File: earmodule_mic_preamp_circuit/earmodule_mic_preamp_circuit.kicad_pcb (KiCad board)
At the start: 2 copper layers, 31.2 x 25.4 mm, 52 parts, among them U100 ADA4661-2ARMZ, U200 AD8476ARMZ, U300 AD8476ARMZ, U400 TITLV71210

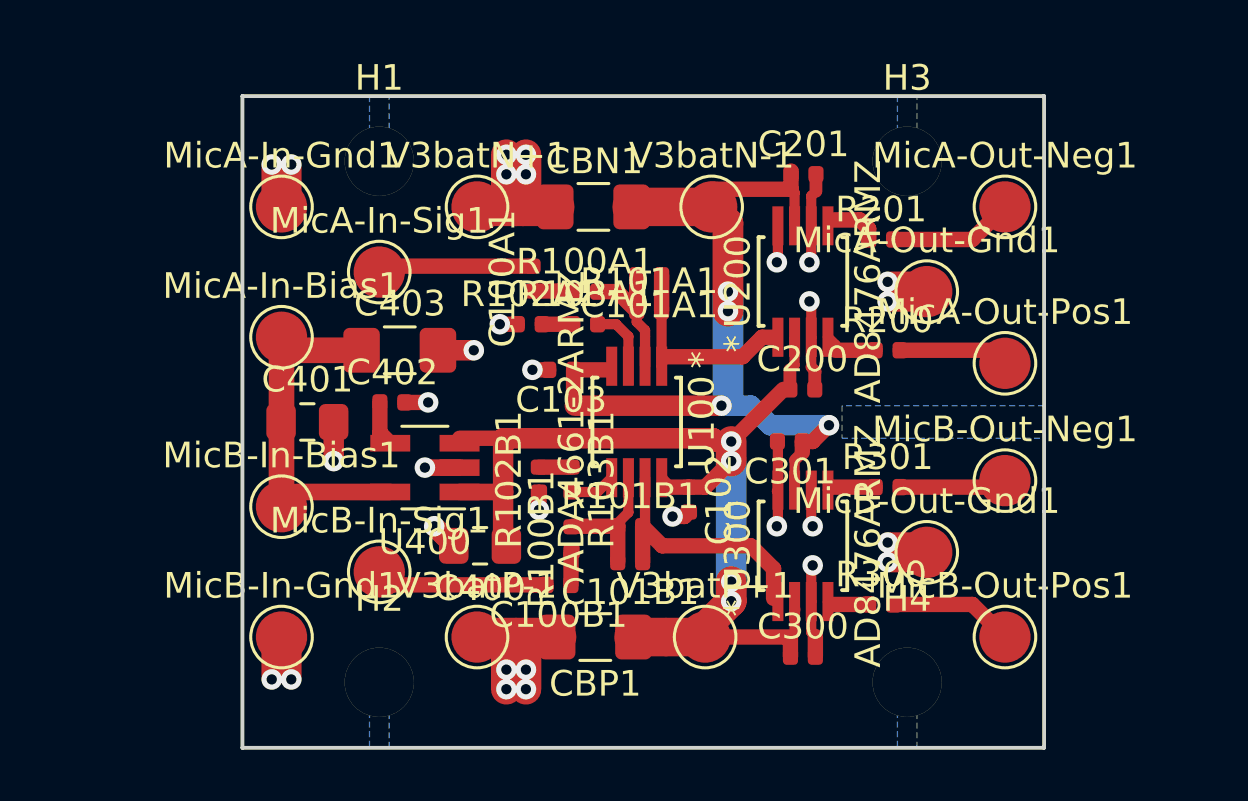
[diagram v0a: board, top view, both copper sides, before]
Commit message: Shrink and position silkscreen
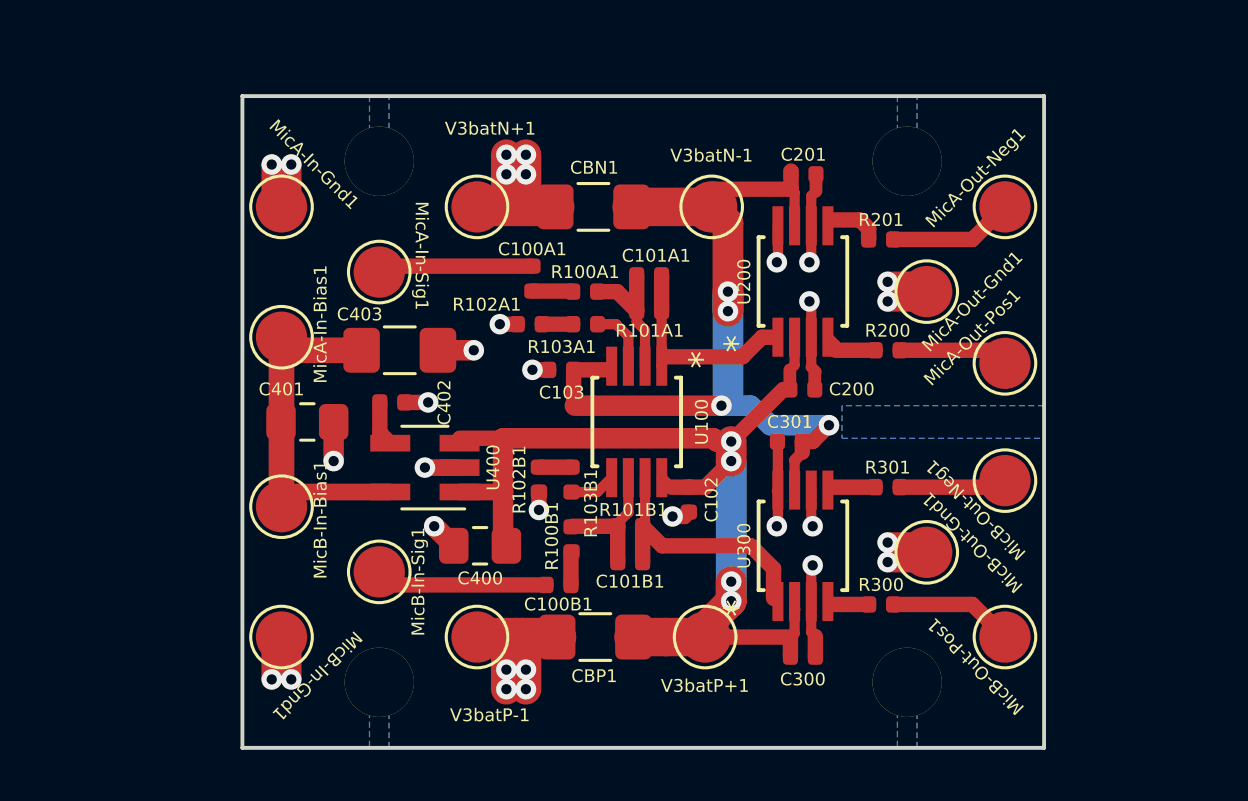
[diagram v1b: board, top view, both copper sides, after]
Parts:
-  : renamed from H4
-  : renamed from H1
-  : renamed from H3
-  : renamed from H2
- U100: value ADA4661-2ARMZ -> RM_8_ADI
- U200, U300: value AD8476ARMZ -> RM_8_ADI

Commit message: Rearranged regulator layout for better co-location of parts. Cleaned up interface names.
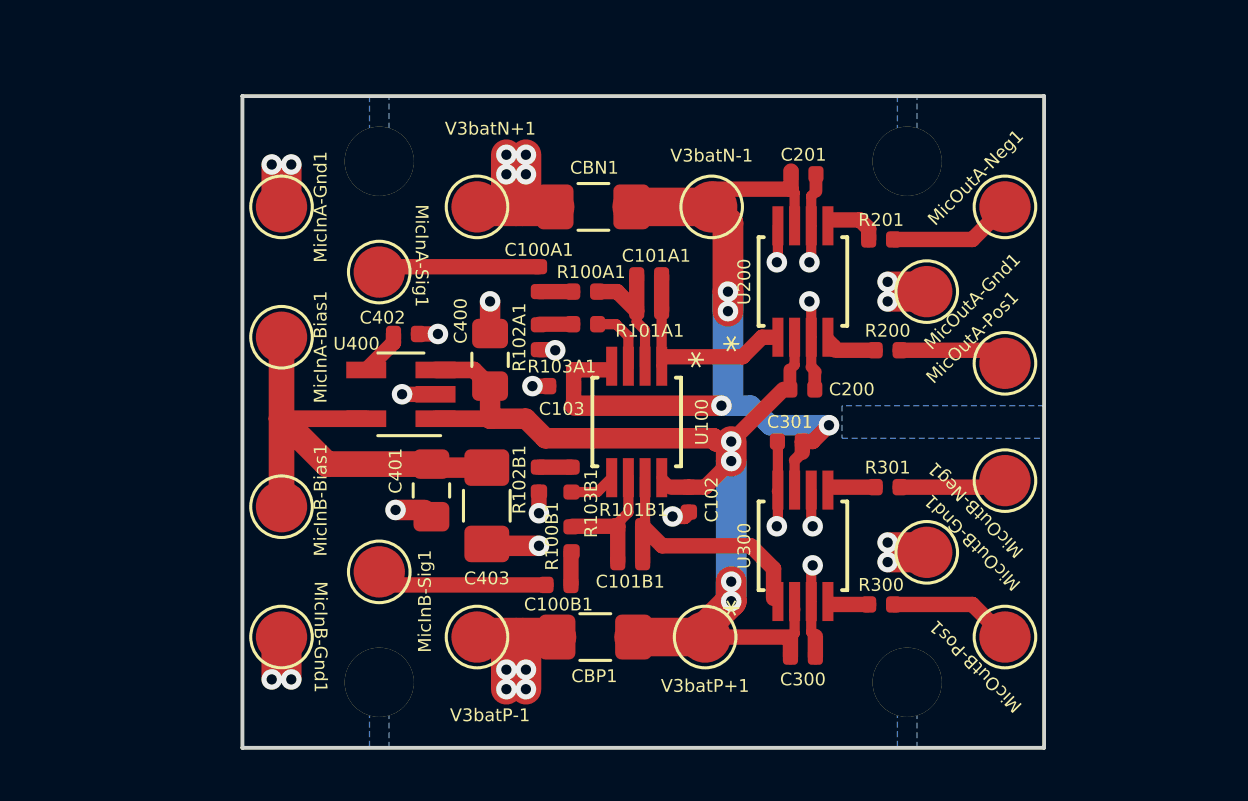
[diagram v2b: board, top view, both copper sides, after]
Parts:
- H1, H2, H3, H4: renamed from  
- U100: value RM_8_ADI -> ADA4661-2ARMZ
- U200, U300: value RM_8_ADI -> AD8476ARMZ
- moved C400 7.26 mm to (122.4, 82.2), turned to 90 degrees
- moved C403 6.94 mm to (122.3, 87.8), turned to 270 degrees
- moved C401 5.52 mm to (120.1, 87.2), turned to 270 degrees
- moved U400 3.00 mm to (119.0, 83.5)
- moved C402 2.72 mm to (119.1, 81.2)
- moved C103 0.64 mm to (125.2, 83.2)
- moved R102A1 0.62 mm to (124.3, 81.3), turned to 90 degrees
- moved C100A1 0.26 mm to (124.3, 79.0)
- renumbered MicA-In-Bias1 to MicInA-Bias1, MicA-In-Gnd1 to MicInA-Gnd1, MicA-In-Sig1 to MicInA-Sig1, MicB-In-Bias1 to MicInB-Bias1, MicB-In-Gnd1 to MicInB-Gnd1, MicB-In-Sig1 to MicInB-Sig1, MicA-Out-Gnd1 to MicOutA-Gnd1, MicA-Out-Neg1 to MicOutA-Neg1, MicA-Out-Pos1 to MicOutA-Pos1, MicB-Out-Gnd1 to MicOutB-Gnd1, MicB-Out-Neg1 to MicOutB-Neg1, MicB-Out-Pos1 to MicOutB-Pos1
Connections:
- net MicA-In-Bias renamed MicInA-Bias
- net MicA-In-Gnd renamed MicInA-Gnd
- net MicA-In-Sig renamed MicInA-Sig
- net MicA-Out-Neg renamed MicOutA-Neg
- net MicA-Out-Pos renamed MicOutA-Pos
- net MicB-In-Sig renamed MicInB-Sig
- net MicB-Out-Neg renamed MicOutB-Neg
- net MicB-Out-Pos renamed MicOutB-Pos
- net V3batN- renamed V3neg
- net V3batP+ renamed V3pos
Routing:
- net MicInA-Bias: track 14.4 -> 19.5 mm
- net V3pos: track 51.4 -> 49.1 mm

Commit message: Enlarged board and wire solder pad sizes. Added small decoupling caps in bias circuit. Finalized naming, numbering, and placement of text.
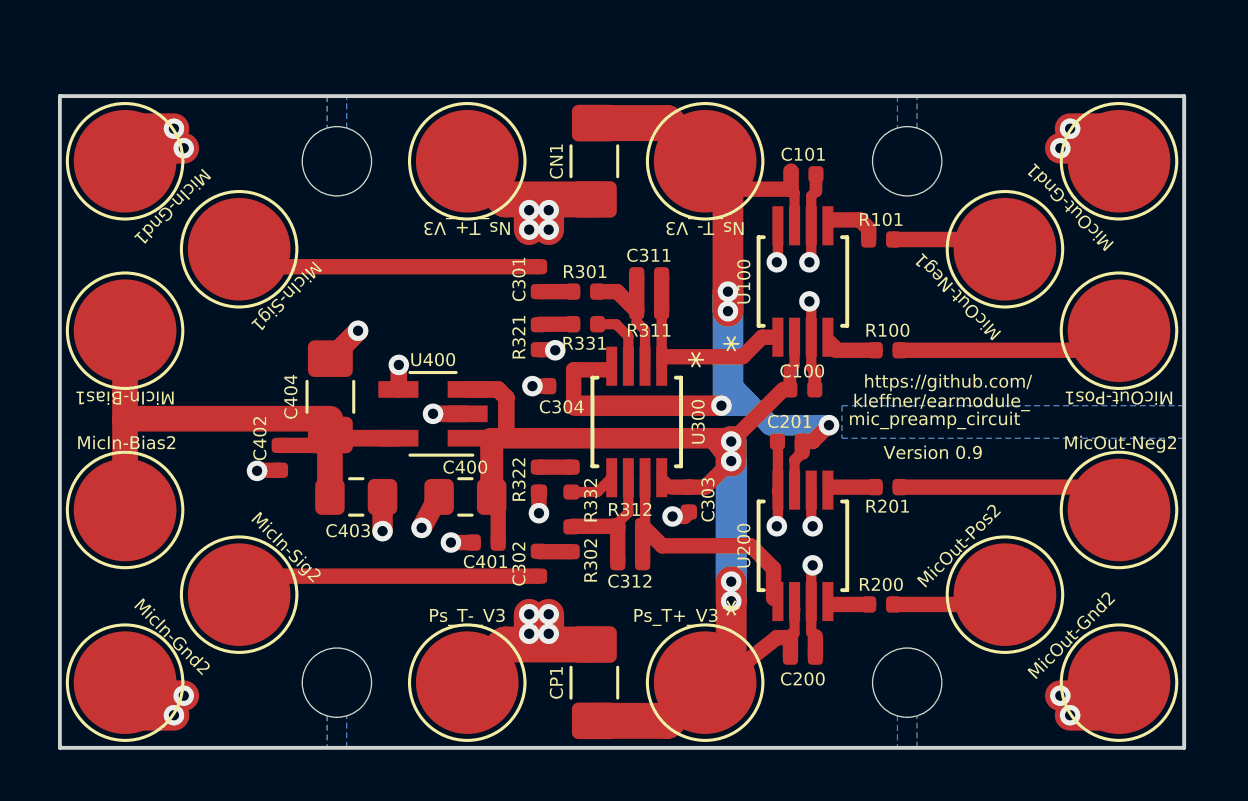
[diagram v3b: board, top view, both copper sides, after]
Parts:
- removed MicInA-Bias1, MicInA-Gnd1, MicInA-Sig1, MicInB-Bias1, MicInB-Gnd1, MicInB-Sig1, MicOutA-Gnd1, MicOutA-Neg1, MicOutA-Pos1, MicOutB-Gnd1, MicOutB-Neg1, MicOutB-Pos1, V3batN+1, V3batN-1, V3batP+1, V3batP-1: Conn_01x01_Male, TestPoint:TestPoint_Pad_D2.0mm
- added C401: 0.1uF, Capacitor_SMD:C_0402_1005Metric, F.Cu at (122.3, 89.3)
- added MicIn-Bias1: Conn_01x01_Male, TestPoint:TestPoint_Pad_D4.0mm, F.Cu at (108.2, 81.0)
- added MicIn-Bias2: Conn_01x01_Male, TestPoint:TestPoint_Pad_D4.0mm, F.Cu at (108.2, 88.0)
- added MicIn-Gnd1: Conn_01x01_Male, TestPoint:TestPoint_Pad_D4.0mm, F.Cu at (108.2, 74.4)
- added MicIn-Gnd2: Conn_01x01_Male, TestPoint:TestPoint_Pad_D4.0mm, F.Cu at (108.2, 94.7)
- added MicIn-Sig1: Conn_01x01_Male, TestPoint:TestPoint_Pad_D4.0mm, F.Cu at (112.6, 77.9)
- added MicIn-Sig2: Conn_01x01_Male, TestPoint:TestPoint_Pad_D4.0mm, F.Cu at (112.6, 91.3)
- added MicOut-Gnd1: Conn_01x01_Male, TestPoint:TestPoint_Pad_D4.0mm, F.Cu at (146.9, 74.4)
- added MicOut-Gnd2: Conn_01x01_Male, TestPoint:TestPoint_Pad_D4.0mm, F.Cu at (146.9, 94.7)
- added MicOut-Neg1: Conn_01x01_Male, TestPoint:TestPoint_Pad_D4.0mm, F.Cu at (142.5, 77.9)
- added MicOut-Neg2: Conn_01x01_Male, TestPoint:TestPoint_Pad_D4.0mm, F.Cu at (146.9, 88.0)
- added MicOut-Pos1: Conn_01x01_Male, TestPoint:TestPoint_Pad_D4.0mm, F.Cu at (146.9, 81.0)
- added MicOut-Pos2: Conn_01x01_Male, TestPoint:TestPoint_Pad_D4.0mm, F.Cu at (142.5, 91.3)
- added Ns_T+_V3: Conn_01x01_Male, TestPoint:TestPoint_Pad_D4.0mm, F.Cu at (121.5, 74.4)
- added Ns_T-_V3: Conn_01x01_Male, TestPoint:TestPoint_Pad_D4.0mm, F.Cu at (130.8, 74.4)
- added Ps_T+_V3: Conn_01x01_Male, TestPoint:TestPoint_Pad_D4.0mm, F.Cu at (130.8, 94.7)
- added Ps_T-_V3: Conn_01x01_Male, TestPoint:TestPoint_Pad_D4.0mm, F.Cu at (121.5, 94.7)
- H1: value Hole1 -> MountingHole
- H2: value Hole2 -> MountingHole
- H3: value Hole3 -> MountingHole
- H4: value Hole4 -> MountingHole
- moved C404 7.43 mm to (116.2, 83.6), turned to 90 degrees
- moved C402 6.89 mm to (114.2, 86.0), turned to 270 degrees
- moved C400 5.43 mm to (121.5, 87.5), turned to 180 degrees
- moved C403 2.94 mm to (117.2, 87.5), turned to 0 degrees
- moved CN1 1.78 mm to (126.5, 74.4), turned to 90 degrees
- moved CP1 1.78 mm to (126.5, 94.7), turned to 90 degrees
- moved H2 1.65 mm to (116.5, 94.7)
- moved H1 1.65 mm to (116.5, 74.4)
- moved U400 1.47 mm to (120.2, 84.3)
- moved C302 1.12 mm to (124.3, 90.1), turned to 270 degrees
- renumbered C200 to C100, C201 to C101, C300 to C200, C301 to C201, C100A1 to C301, C100B1 to C302, C102 to C303, C103 to C304, C101A1 to C311, C101B1 to C312, C401 to C403, C403 to C404, CBN1 to CN1, CBP1 to CP1, R200 to R100, R201 to R101, R300 to R200, R301 to R201, R100A1 to R301, R100B1 to R302, R101A1 to R311, R101B1 to R312, R102A1 to R321, R102B1 to R322, R103A1 to R331, R103B1 to R332, U200 to U100, U300 to U200, U100 to U300
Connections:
- C100 pad 2: MicInA-Gnd -> GNDA
- C101 pad 2: MicInA-Gnd -> GNDA
- C200 pad 2: MicInA-Gnd -> GNDA
- C201 pad 2: MicInA-Gnd -> GNDA
- C301 pad 2: MicInA-Sig -> Net-(C301-Pad2)
- C302 pad 2: MicInB-Sig -> Net-(C302-Pad2)
- C303 pad 2: MicInA-Gnd -> GNDA
- C304 pad 2: MicInA-Gnd -> GNDA
- C400 pad 2: MicInA-Gnd -> GNDA
- C402 pad 2: MicInA-Gnd -> GNDA
- C403 pad 1: MicInA-Bias -> Net-(C402-Pad1)
- C403 pad 2: MicInA-Gnd -> GNDA
- C404 pad 1: MicInA-Bias -> Net-(C402-Pad1)
- C404 pad 2: MicInA-Gnd -> GNDA
- CN1 pad 1: MicInA-Gnd -> GNDA
- CP1 pad 2: MicInA-Gnd -> GNDA
- R100 pad 2: MicOutA-Pos -> Net-(MicOut-Pos1-Pad1)
- R101 pad 2: MicOutA-Neg -> Net-(MicOut-Neg1-Pad1)
- R200 pad 2: MicOutB-Pos -> Net-(MicOut-Pos2-Pad1)
- R201 pad 2: MicOutB-Neg -> Net-(MicOut-Neg2-Pad1)
- R321 pad 1: MicInA-Gnd -> GNDA
- R322 pad 1: MicInA-Gnd -> GNDA
- U100 pad 3: MicInA-Gnd -> GNDA
- U100 pad 6: MicInA-Gnd -> GNDA
- U100 pad 8: MicInA-Gnd -> GNDA
- U200 pad 3: MicInA-Gnd -> GNDA
- U200 pad 6: MicInA-Gnd -> GNDA
- U200 pad 8: MicInA-Gnd -> GNDA
- U400 pad 2: MicInA-Gnd -> GNDA
- U400 pad 4: Net-(C402-Pad1) -> GNDA
- U400 pad 5: MicInA-Bias -> Net-(C402-Pad1)
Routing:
- net GNDA: track 0.00 -> 58.9 mm, vias 0 -> 33
- net MicInA-Gnd: track 56.1 -> 0.00 mm, vias 31 -> 0
- net Net-(C402-Pad1): track 1.84 -> 21.9 mm
- net MicInA-Bias: track 19.5 -> 0.00 mm
- net Net-(C302-Pad2): track 0.00 -> 11.7 mm
- net Net-(C301-Pad2): track 0.00 -> 11.7 mm
- net Net-(MicOut-Pos1-Pad1): track 0.00 -> 8.53 mm
- net Net-(MicOut-Neg2-Pad1): track 0.00 -> 8.53 mm
- net MicInB-Sig: track 6.71 -> 0.00 mm
- net MicInA-Sig: track 6.31 -> 0.00 mm
- net MicOutB-Pos: track 4.87 -> 0.00 mm
- net MicOutA-Neg: track 4.87 -> 0.00 mm
- net V3neg: track 33.8 -> 38.4 mm
- net Net-(MicOut-Pos2-Pad1): track 0.00 -> 4.34 mm
- net Net-(MicOut-Neg1-Pad1): track 0.00 -> 4.34 mm
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- added copper zone on B.Cu, net GNDA
- removed copper zone on B.Cu, net MicInA-Gnd
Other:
- board size 31.2 x 25.4 mm -> 43.8 x 25.4 mm
- board text added: "Version 0.9"
- board text added: "https://github.com/"
- board text added: "kleffner/earmodule_"
- board text added: "mic_preamp_circuit"
